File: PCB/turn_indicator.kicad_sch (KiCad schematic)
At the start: 18 parts

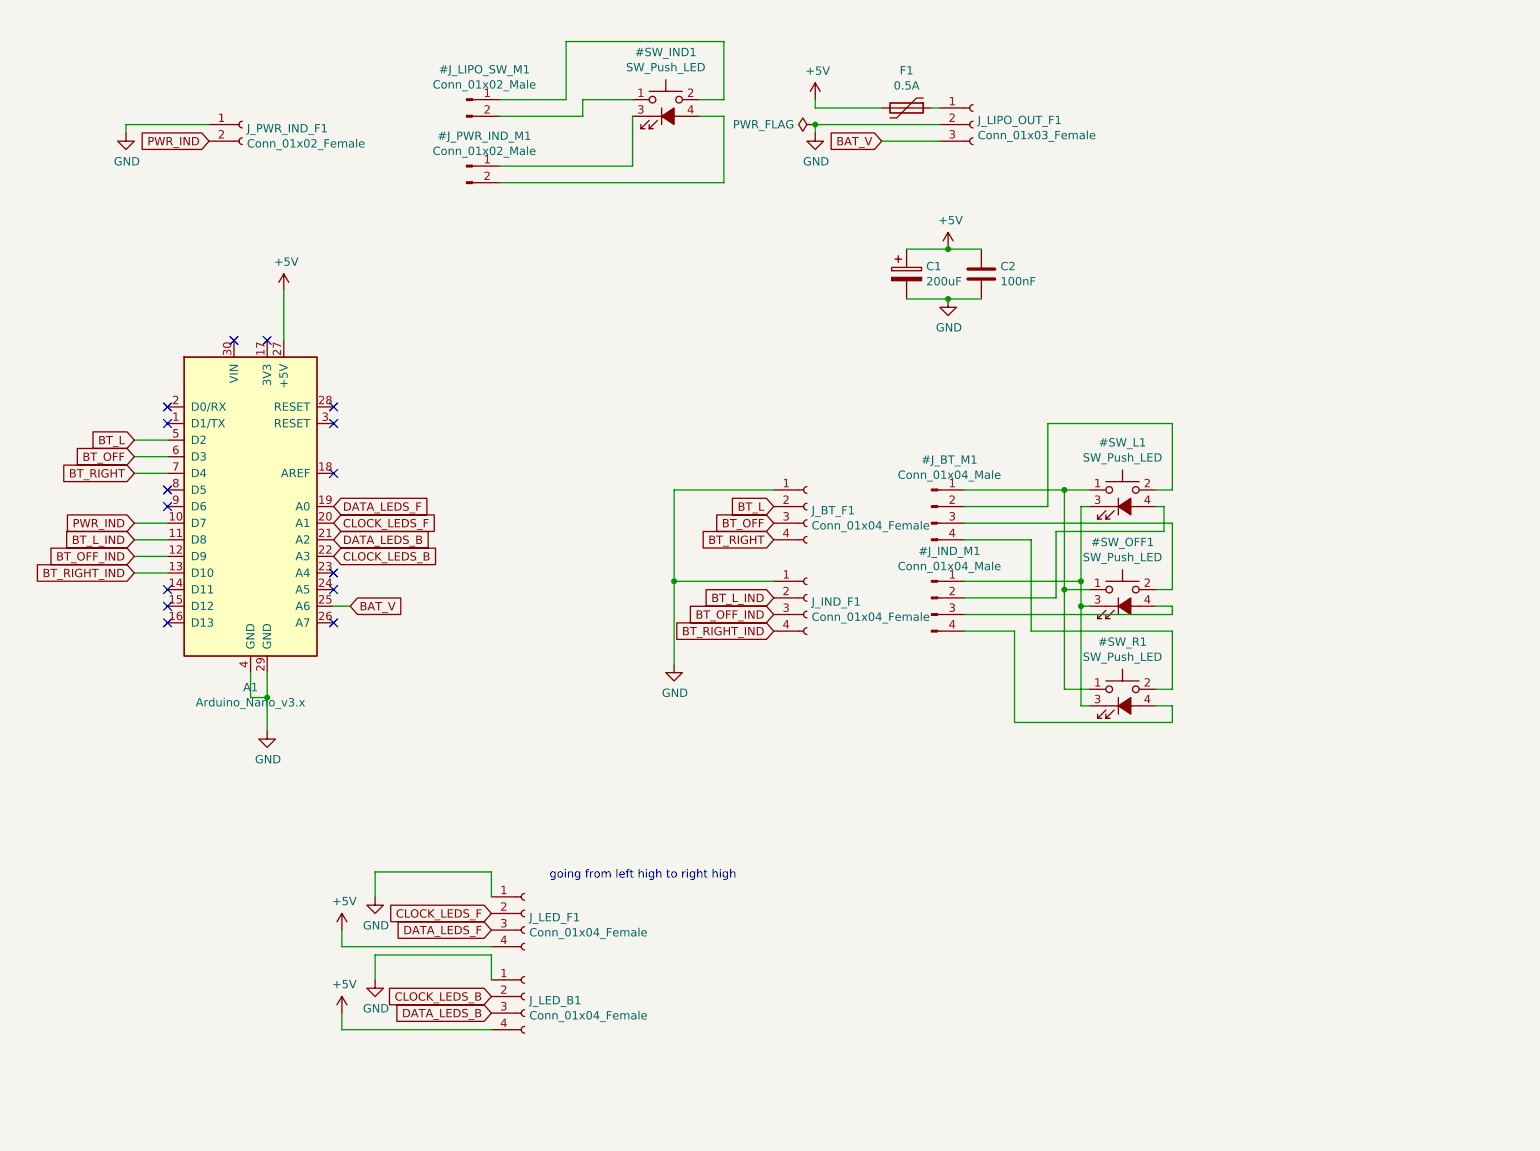
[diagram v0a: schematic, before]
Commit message: update to kicad 7, increase fuse size to proper 1206, cleanup PCB, include QR code and MF logo
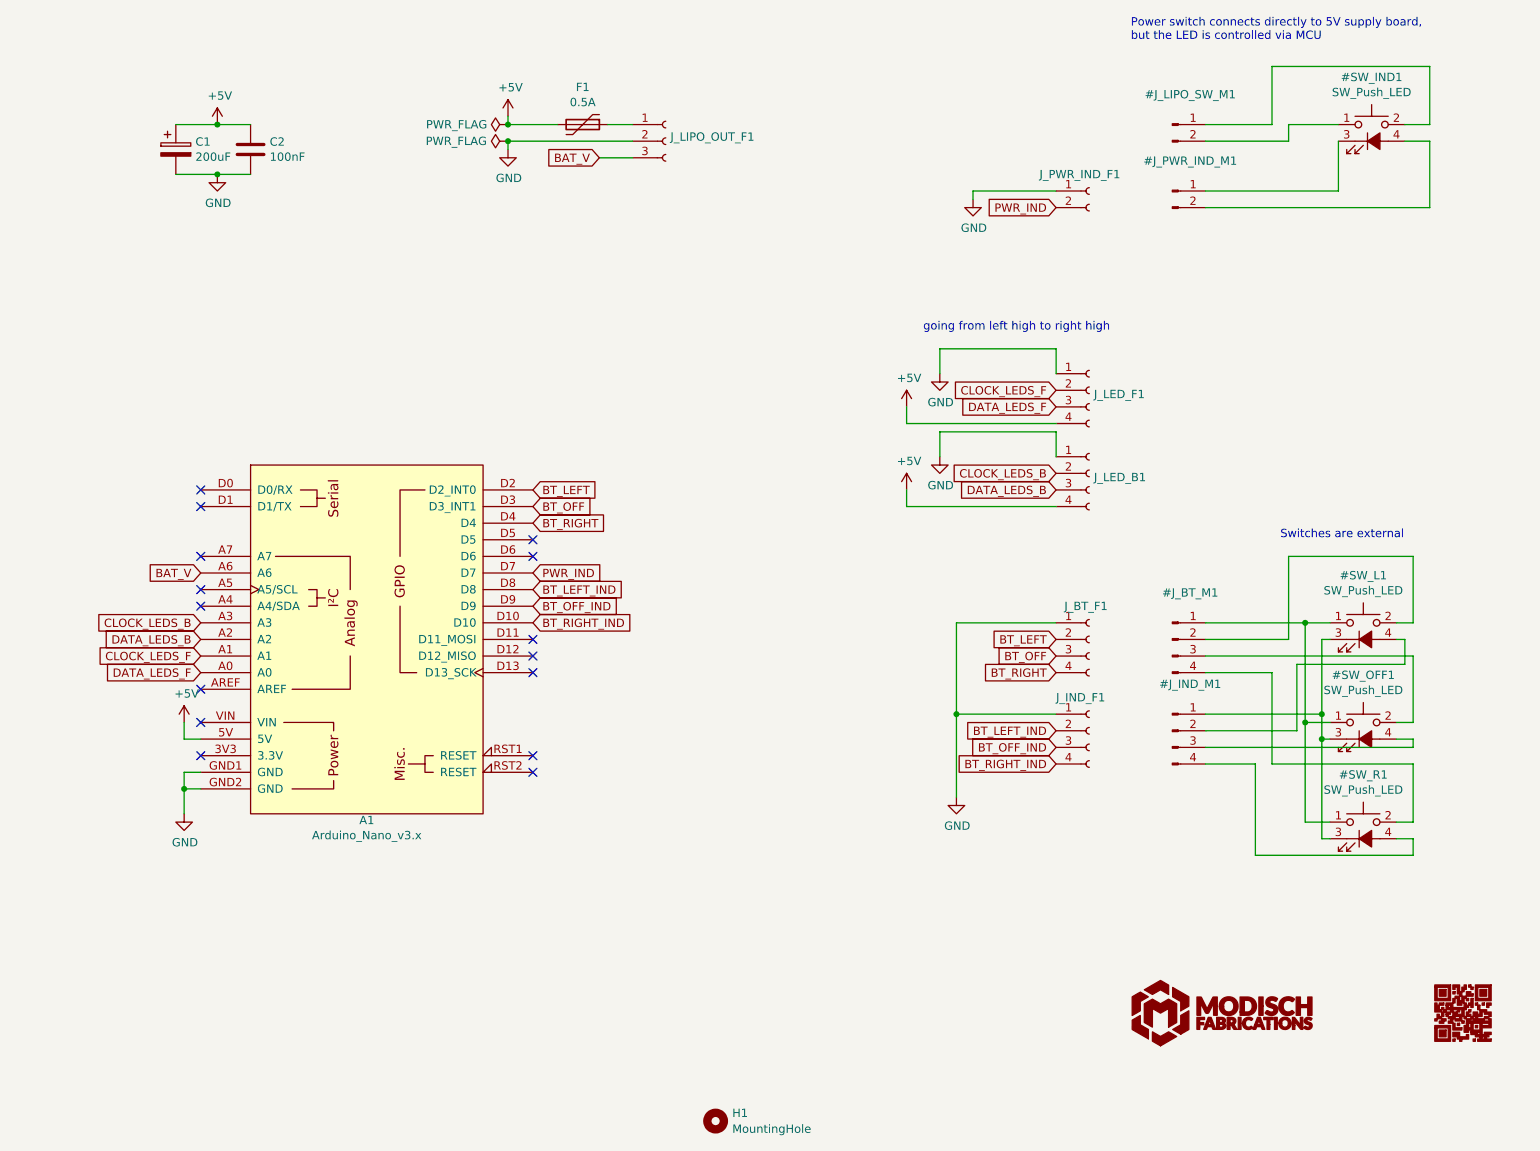
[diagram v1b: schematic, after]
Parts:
- added H1: MountingHole, MountingHole:MountingHole_3.2mm_M3, symbol Mechanical:MountingHole
- #J_BT_M1, #J_IND_M1: value Conn_01x04_Male -> Conn_01x04_Pin; symbol Connector:Conn_01x04_Male -> Connector:Conn_01x04_Pin
- #J_LIPO_SW_M1, #J_PWR_IND_M1: value Conn_01x02_Male -> Conn_01x02_Pin; symbol Connector:Conn_01x02_Male -> Connector:Conn_01x02_Pin
- A1: footprint Module:Arduino_Nano -> PCM_arduino-library:Arduino_Nano_Socket; symbol turn_indicator-rescue:Arduino_Nano_v3.x-MCU_Module -> PCM_arduino-library:Arduino_Nano_Socket
- C1: symbol turn_indicator-rescue:CP-Device -> Device:C_Polarized
- F1: footprint Fuse:Fuse_0805_2012Metric -> Fuse:Fuse_1206_3216Metric_Pad1.42x1.75mm_HandSolder
- J_BT_F1, J_IND_F1, J_LED_B1, J_LED_F1: value Conn_01x04_Female -> Conn_01x04_Socket; symbol Connector:Conn_01x04_Female -> Connector:Conn_01x04_Socket
- J_LIPO_OUT_F1: value Conn_01x03_Female -> Conn_01x03_Socket; symbol Connector:Conn_01x03_Female -> Connector:Conn_01x03_Socket
- J_PWR_IND_F1: value Conn_01x02_Female -> Conn_01x02_Socket; symbol Connector:Conn_01x02_Female -> Connector:Conn_01x02_Socket
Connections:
- net +5V: now also A1.5V; no longer A1.27 (+5V)
- net BAT_V: now also A1.A6; no longer A1.25 (A6)
- net BT_OFF: now also A1.D3 (D3_INT1); no longer A1.6 (D3)
- net BT_OFF_IND: now also A1.D9; no longer A1.12 (D9)
- net BT_RIGHT: now also A1.D4; no longer A1.7 (D4)
- net BT_RIGHT_IND: now also A1.D10; no longer A1.13 (D10)
- net CLOCK_LEDS_B: now also A1.A3; no longer A1.22 (A3)
- net CLOCK_LEDS_F: now also A1.A1; no longer A1.20 (A1)
- net DATA_LEDS_B: now also A1.A2; no longer A1.21 (A2)
- net DATA_LEDS_F: now also A1.A0; no longer A1.19 (A0)
- net GND: now also A1.GND1 (GND), A1.GND2 (GND); no longer A1.29 (GND), A1.4 (GND)
- net PWR_IND: now also A1.D7; no longer A1.10 (D7)
- net BT_L renamed BT_LEFT
- net BT_LEFT: now also A1.D2 (D2_INT0); no longer A1.5 (D2)
- net BT_L_IND renamed BT_LEFT_IND
- net BT_LEFT_IND: now also A1.D8; no longer A1.11 (D8)
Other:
- note added: "Power switch connects directly to 5V supply board, but the LED is controlled via MCU"
- note added: "Switches are external"
- company: (none) -> Modisch Fabrications
- title: (none) -> Turn Indicator
- moved on the sheet: C1, C2, F1, J_BT_F1, J_IND_F1, J_LED_B1, J_LED_F1, J_LIPO_OUT_F1, J_PWR_IND_F1
